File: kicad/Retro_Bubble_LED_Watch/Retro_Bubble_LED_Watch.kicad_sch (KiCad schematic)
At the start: 31 parts, among them J1 USB_C_Receptacle, J2 Conn_02x03_Odd_Even, Q1 BC547, Q2 BC547, Q3 BC547, Q4 BC547, Q5 BC547, SW1 SW_Push, SW2 SW_Push, U1 ATmega328PB-A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

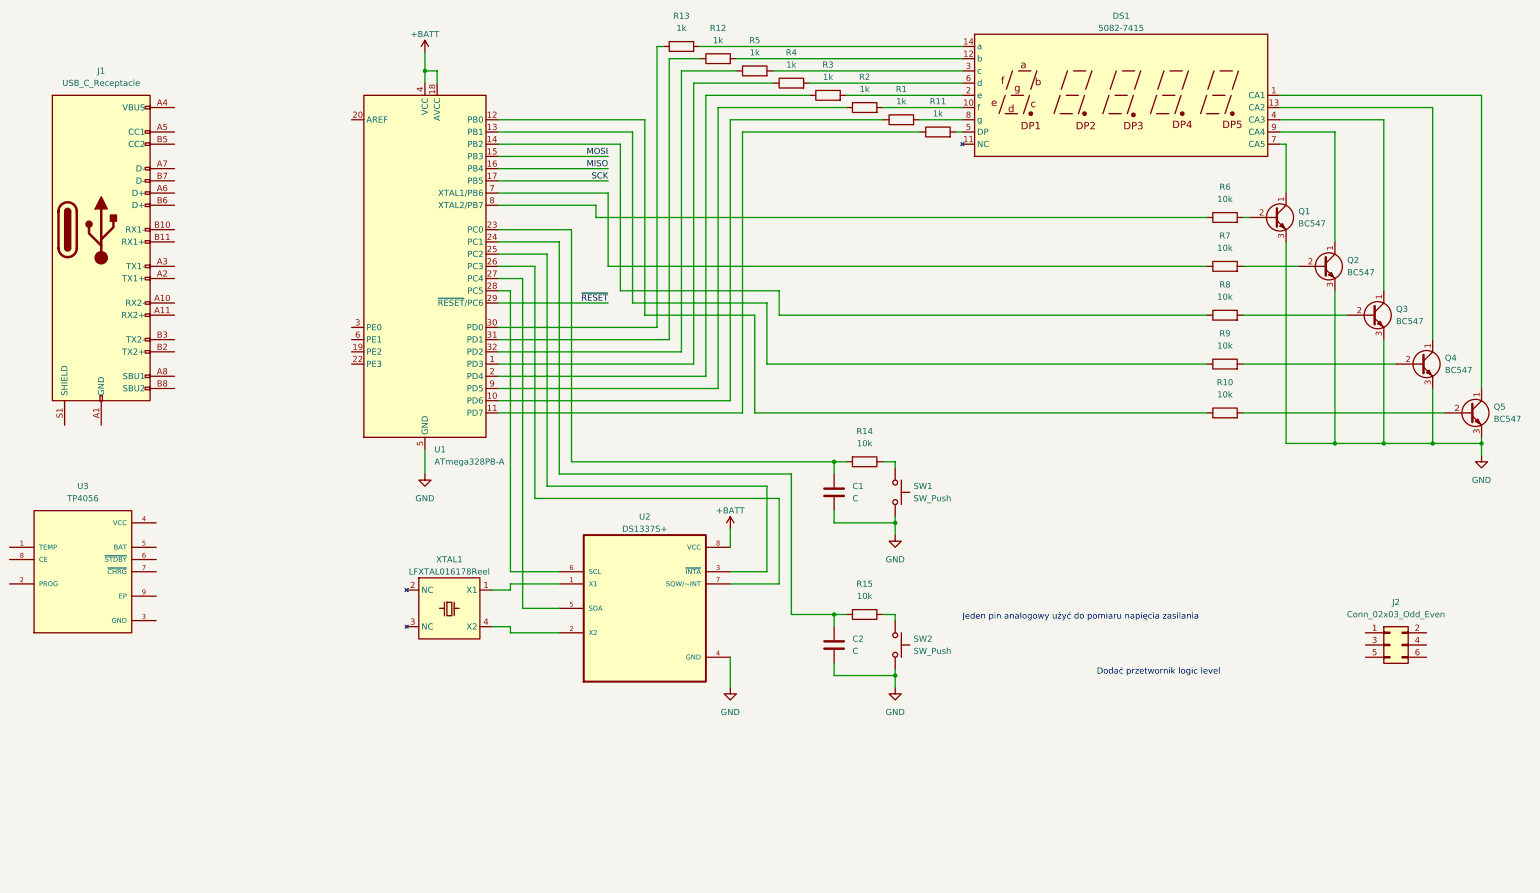
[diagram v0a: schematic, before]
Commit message: restructurized code with structs
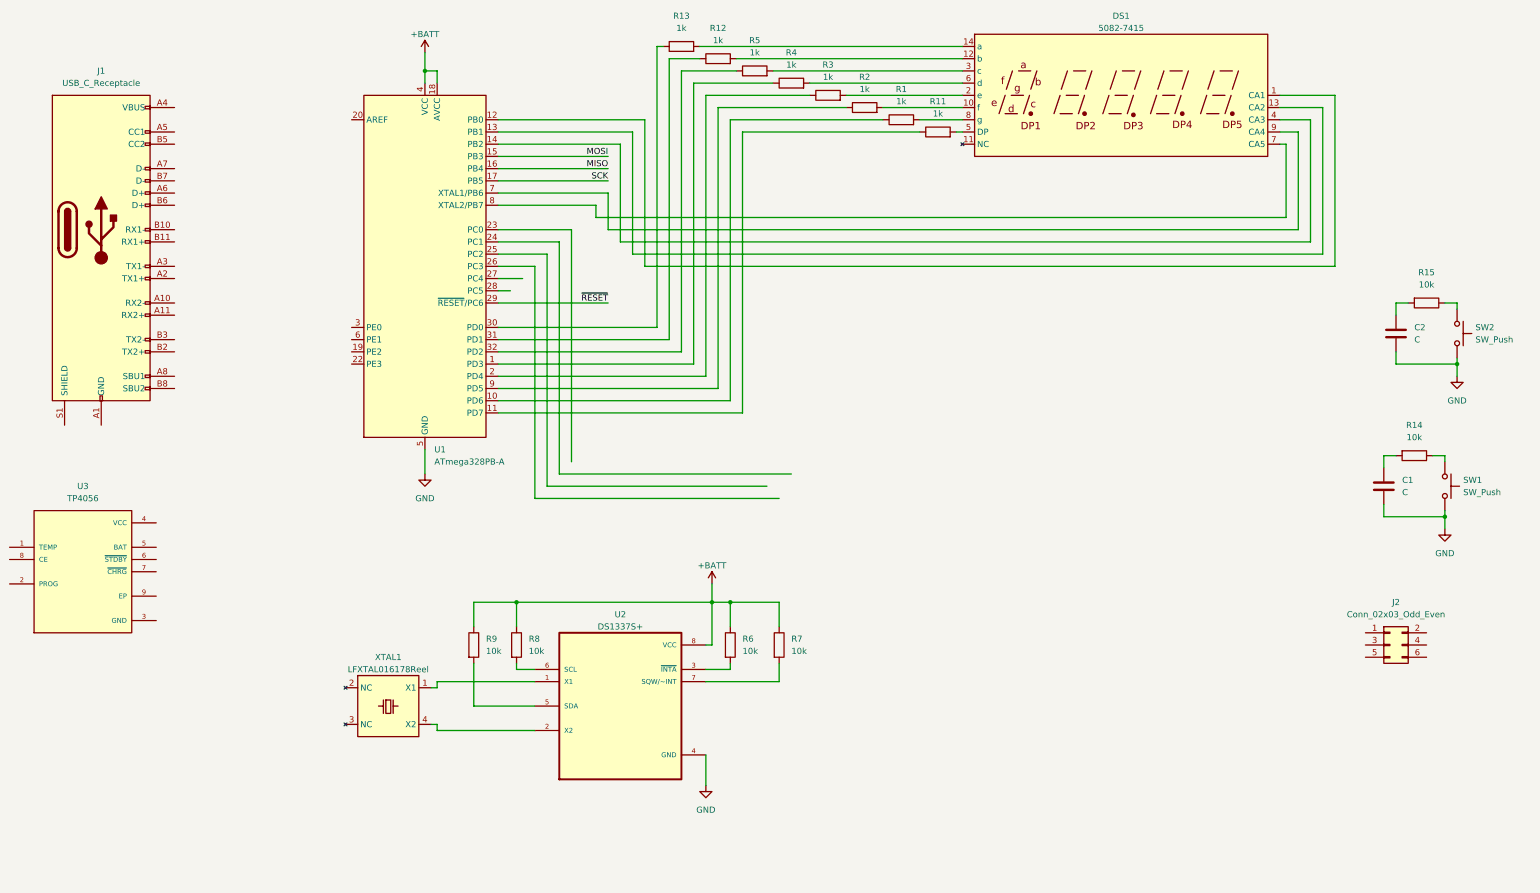
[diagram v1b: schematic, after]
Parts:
- removed Q1, Q2, Q3, Q4, Q5: BC547, Package_TO_SOT_THT:TO-92_Inline, symbol Transistor_BJT:BC547
- removed R10: 10k, Resistor_SMD:R_0805_2012Metric, symbol Device:R
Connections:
- net +BATT: now also R6.1, R7.1, R8.1, R9.1
- net at U1.14 (PB2): now also DS1.4 (CA3); no longer R8.1
- net at R8.2: now also U2.6 (SCL)
- net at DS1.13 (CA2): now also U1.13 (PB1)
- net at R9.2: now also U2.5 (SDA)
- net at U1.12 (PB0): now also DS1.1 (CA1)
- net at DS1.9 (CA4): now also U1.7 (XTAL1/PB6)
- net at R7.2: now also U2.7 (SQW/~INT)
- net at C1.1, R14.2: no longer U1.23 (PC0)
- net at C2.1, R15.2: no longer U1.24 (PC1)
- net at U2.3 (~{INTA}): now also R6.2; no longer U1.25 (PC2)
- net at U1.26 (PC3): no longer U2.7 (SQW/~INT)
- net at U1.27 (PC4): no longer U2.5 (SDA)
- net at U1.28 (PC5): no longer U2.6 (SCL)
- net at U1.8 (XTAL2/PB7): now also DS1.7 (CA5); no longer R6.1
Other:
- note removed: "Dodać przetwornik logic level"
- note removed: "Jeden pin analogowy użyć do pomiaru napięcia zasilania"
- moved on the sheet: C1, C2, R14, R15, SW1, SW2, U2, XTAL1

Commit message: added sleep mode
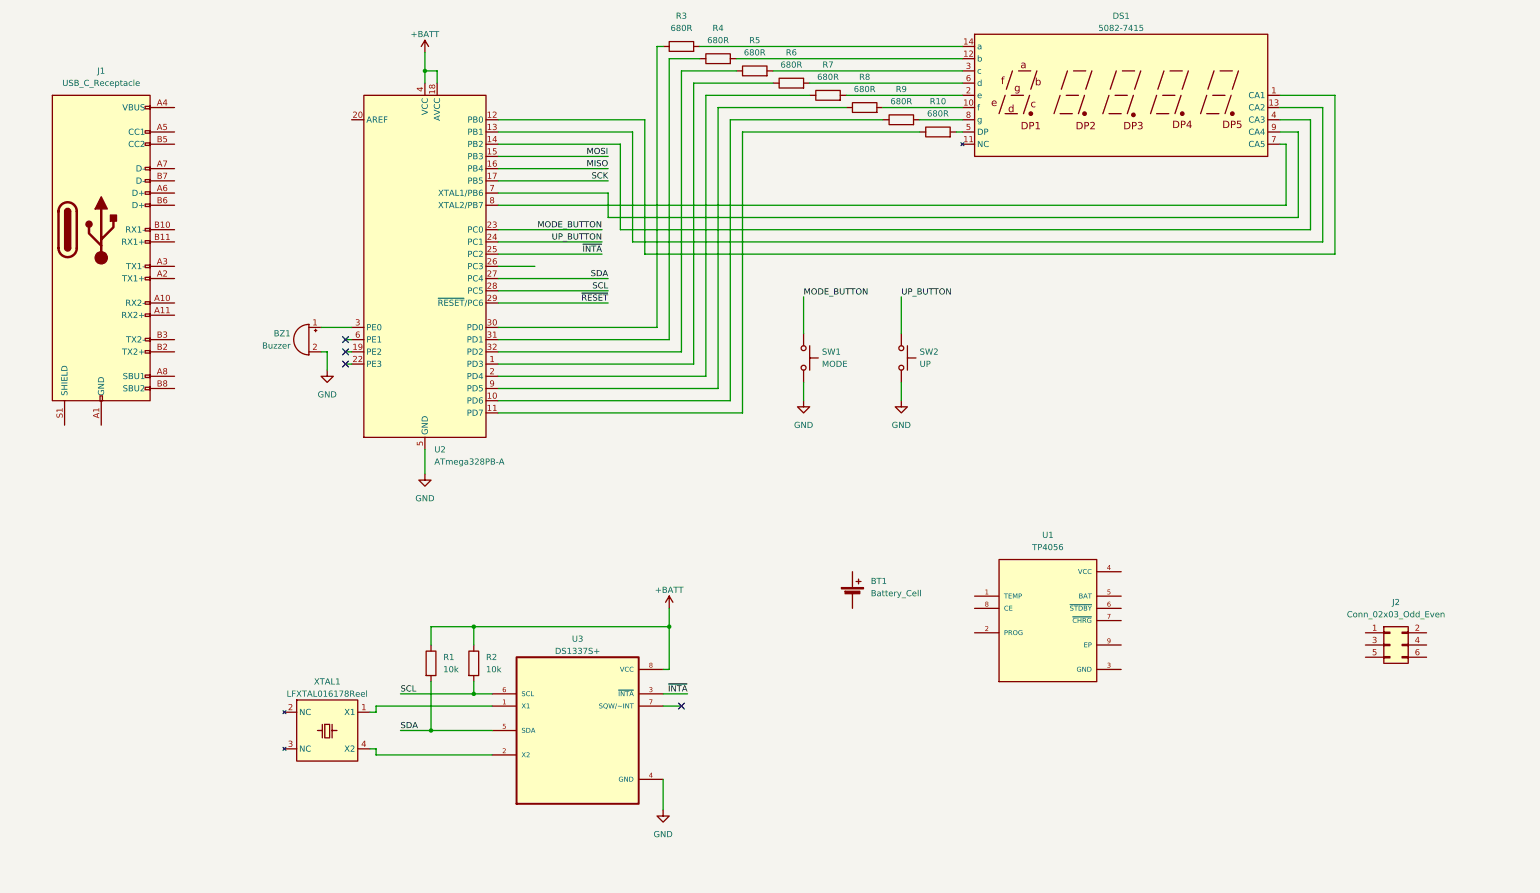
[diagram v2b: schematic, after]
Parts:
- removed C1, C2: C, symbol Device:C
- removed R14, R15, R6, R7: 10k, Resistor_SMD:R_0805_2012Metric, symbol Device:R
- added BT1: Battery_Cell, symbol Device:Battery_Cell
- added BZ1: Buzzer, symbol Device:Buzzer
- R10: renamed from R11; value 1k -> 680R
- R3: renamed from R13; value 1k -> 680R
- R4: renamed from R12; value 1k -> 680R
- R5: value 1k -> 680R
- R6: renamed from R4; value 1k -> 680R
- R7: renamed from R3; value 1k -> 680R
- R8: renamed from R2; value 1k -> 680R
- R9: renamed from R1; value 1k -> 680R
- SW1: value SW_Push -> MODE
- SW2: value SW_Push -> UP
- renumbered R9 to R1, R8 to R2, U3 to U1, U1 to U2, U2 to U3
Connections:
- net GND: now also BZ1.2 (-)
- net ~{INTA}: now reaches U3.3 (~{INTA})
- net ~{INTA}: now also U2.25 (PC2)
- net MODE_BUTTON: now reaches U2.23 (PC0)
- net MODE_BUTTON: now also SW1.1
- net UP_BUTTON: now reaches U2.24 (PC1)
- net UP_BUTTON: now also SW2.1
- net SDA: now reaches U2.27 (PC4)
- net SDA: now also R1.2, U3.5 (SDA)
- net SCL: now reaches U2.28 (PC5)
- net SCL: now also R2.2, U3.6 (SCL)
- net at U2.3 (PE0): now also BZ1.1 (+)
- no-connect marks 0 -> 4
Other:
- moved on the sheet: R1, R2, SW1, SW2, U1, U3, XTAL1

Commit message: fixed 2nd alarm
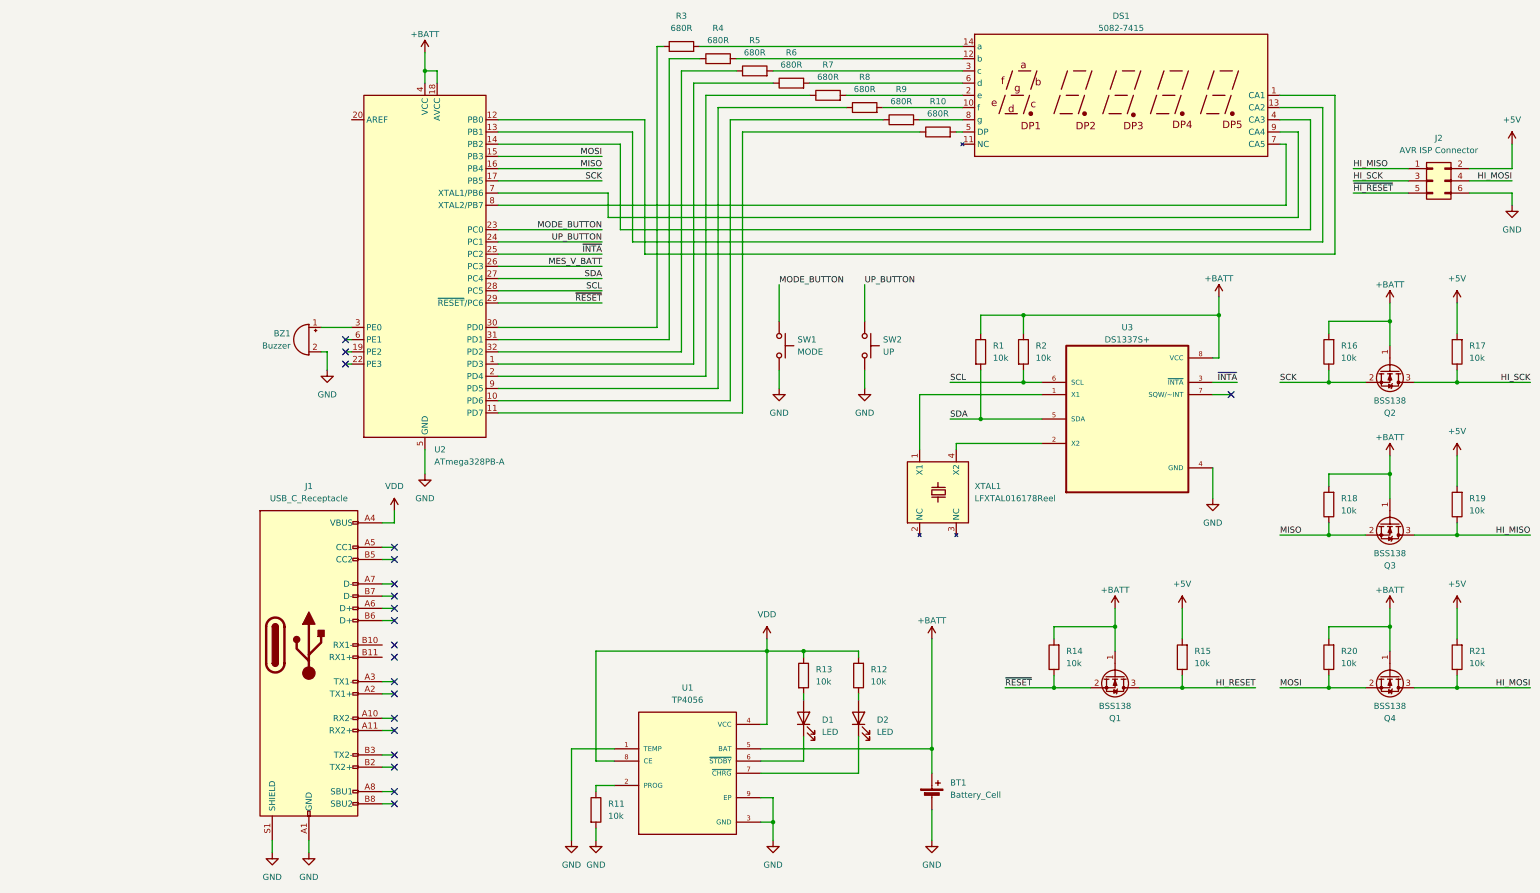
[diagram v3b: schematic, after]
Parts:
- added D1, D2: LED, symbol Device:LED
- added Q1, Q2, Q3, Q4: BSS138, Package_TO_SOT_SMD:SOT-23, symbol Transistor_FET:BSS138
- added R11, R12, R13, R14, R15, R16, R17, R18, R19, R20, R21: 10k, Resistor_SMD:R_0805_2012Metric, symbol Device:R
- J1: footprint (none) -> Connector_USB:USB_C_Receptacle_G-Switch_GT-USB-7010ASV
- J2: value Conn_02x03_Odd_Even -> AVR ISP Connector; footprint (none) -> Connector_PinHeader_2.54mm:PinHeader_2x03_P2.54mm_Vertical
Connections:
- net +BATT: now also BT1.1 (+), U1.5 (BAT), Q1.1 (G), Q2.1 (G), Q3.1 (G), Q4.1 (G), R14.2, R16.2, R18.2, R20.2
- net GND: now also BT1.2 (-), J1.A1 (GND), J1.A12 (GND), J1.B1 (GND), J1.B12 (GND), J1.S1 (SHIELD), J2.6 (Pin_6), U1.1 (TEMP), U1.3 (GND), U1.9 (EP), R11.2
- net MISO: now also Q3.2 (S), R18.1
- net MOSI: now also Q4.2 (S), R20.1
- net SCK: now also Q2.2 (S), R16.1
- net ~{RESET}: now also Q1.2 (S), R14.1
- net MES_V_BATT: now reaches U2.26 (PC3)
- net HI_MISO: now reaches J2.1 (Pin_1)
- net HI_MISO: now also Q3.3 (D), R19.1
- net +5V: now reaches J2.2 (Pin_2)
- net +5V: now also R15.2, R17.2, R19.2, R21.2
- net HI_SCK: now reaches J2.3 (Pin_3)
- net HI_SCK: now also Q2.3 (D), R17.1
- net HI_MOSI: now reaches J2.4 (Pin_4)
- net HI_MOSI: now also Q4.3 (D), R21.1
- net ~{HI_RESET}: now reaches J2.5 (Pin_5)
- net at U1.2 (PROG): now also R11.1
- net VDD: now reaches U1.4 (VCC)
- net VDD: now also J1.A4 (VBUS), J1.A9 (VBUS), J1.B4 (VBUS), J1.B9 (VBUS), U1.8 (CE), R12.2, R13.1
- net at U1.6 (~{STDBY}): now also D1.1 (K)
- net at U1.7 (~{CHRG}): now also D2.1 (K)
- new net: D2.2 (A), R12.1
- new net: D1.2 (A), R13.2
- new net HI_RESET: Q1.3 (D), R15.1
- no-connect marks 4 -> 20
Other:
- moved on the sheet: BT1, J1, J2, R1, R2, SW1, SW2, U1, U3, XTAL1

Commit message: changed energy source to cr2032 battery
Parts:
- removed D1, D2: LED, symbol Device:LED
- removed J1: USB_C_Receptacle, Connector_USB:USB_C_Receptacle_G-Switch_GT-USB-7010ASV, symbol Connector:USB_C_Receptacle
- removed R11, R12, R13: 10k, Resistor_SMD:R_0805_2012Metric, symbol Device:R
- removed U1: TP4056, TP4056:SOP127P600X175-9N, symbol TP4056:TP4056
- added C1: 100n, Capacitor_SMD:C_0603_1608Metric, symbol Device:C
- BT1: value Battery_Cell -> Panasonic CR2032; footprint (none) -> Battery:BatteryHolder_Keystone_1058_1x2032
- BZ1: footprint (none) -> Buzzer_Beeper:Buzzer_Murata_PKLCS1212E
- DS1: footprint Package_DIP:DIP-14_W7.62mm -> Package_DIP:DIP-14_W8.89mm_SMDSocket_LongPads
- R1, R10, R14, R15, R16, R17, R18, R19, R2, R20, R21, R3, R4, R5, R6, R7, R8, R9: footprint Resistor_SMD:R_0805_2012Metric -> Resistor_SMD:R_0603_1608Metric
- SW1, SW2: footprint (none) -> Button_Switch_SMD:SW_SPST_CK_KMS2xxG
- XTAL1: footprint (none) -> Crystal:Crystal_SMD_SeikoEpson_MC306-4Pin_8.0x3.2mm_HandSoldering
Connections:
- net +BATT: now also C1.1
- net GND: now also C1.2
- net MES_V_BATT: no longer names the net of U2.26 (PC3)
- no-connect marks 20 -> 6
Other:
- moved on the sheet: BT1, J2, Q1, Q2, Q3, Q4, R1, R14, R15, R16, R17, R18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
